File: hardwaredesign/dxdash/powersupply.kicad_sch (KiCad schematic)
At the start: 20 parts, among them J3 12V_in, U4 AMS1117-3.3, U5 TPS54302

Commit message: controller board added features
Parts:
- removed JP1: SolderJumper3V3together, Jumper:SolderJumper-2_P1.3mm_Open_TrianglePad1.0x1.5mm, symbol Jumper:SolderJumper_2_Open
- added C1: 100n, Capacitor_SMD:C_1206_3216Metric_Pad1.33x1.80mm_HandSolder, symbol Device:C_Small
- added Q7: BC556, Package_TO_SOT_THT:TO-92_Inline, symbol Transistor_BJT:BC556
- added Q8: BC546, Package_TO_SOT_THT:TO-92_Inline, symbol Transistor_BJT:BC546
- added R10, R7, R9: 4k7, Resistor_SMD:R_1206_3216Metric_Pad1.30x1.75mm_HandSolder, symbol Device:R_Small
- added R11, R12, R8: 10k, Resistor_SMD:R_1206_3216Metric_Pad1.30x1.75mm_HandSolder, symbol Device:R_Small
- added SW1: SW_Push, Button_Switch_THT:SW_PUSH_6mm_H5mm, symbol Switch:SW_Push
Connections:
- net 24V_P: now also Q7.3 (E), R9.2; no longer C67.2, U5.3 (VIN)
- net GND: now also C1.1, Q8.3 (E), R12.2, SW1.1
- new net: Q7.2 (B), R10.1, R7.2, R9.1
- new net: Q8.1 (C), R7.1
- new net: Q8.2 (B), R8.1
- new net: R10.2, R11.2, SW1.2
- new net 24V_SWITCHED: C67.2, Q7.1 (C), U5.3 (VIN)
- new net KEEP_ON: R8.2
- new net uC_pwr_button: C1.2, R11.1, R12.1
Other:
- note added: "power on/off circuit. For power-on, the power button activates the supply. The controller then can keep the power active by setting KEEP_ON. For power-off, the controller reads the power-button via a digital input, and turns-off the KEEP_ON after the button is released."
- moved on the sheet: C57, C64, C65, C66, C67, C68, C69, C70, C71, D9, J3, L13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

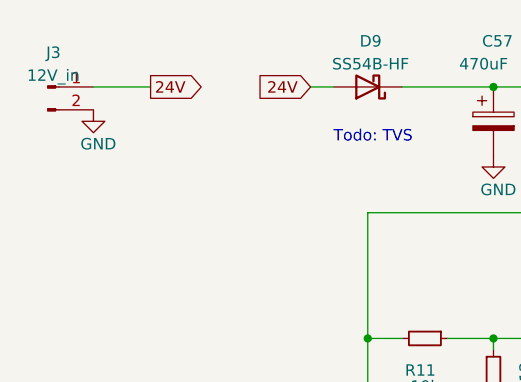
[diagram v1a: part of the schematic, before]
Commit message: added switch inputs. Layout preparation.
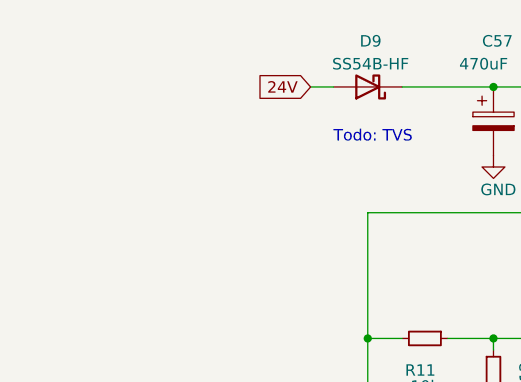
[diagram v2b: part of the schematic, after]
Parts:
- removed J3: 12V_in, Connector_PinHeader_2.54mm:PinHeader_1x02_P2.54mm_Vertical, symbol Connector:Conn_01x02_Pin
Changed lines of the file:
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@@
 	(wire
 		(pts
-			(xy 27.94 25.4) (xy 34.29 25.4)
-		)
-		(stroke
-			(width 0)
-			(type default)
-		)
-	)
-	(wire
-		(pts
 			(xy 142.24 39.37) (xy 142.24 44.45)
 		)
@@
 		)
 	)
-	(global_label "24V"
-		(shape output)
-		(at 34.29 25.4 0)
-		(fields_autoplaced yes)
-		(effects
-			(font
-				(size 1.27 1.27)
-			)
-			(justify left)
-		)
-		(property "Intersheetrefs" "${INTERSHEET_REFS}"
-			(at 40.7828 25.4 0)
-			(effects
-				(font
-					(size 1.27 1.27)
-				)
-				(justify left)
-				(hide yes)
-			)
-		)
-	)
 	(global_label "24V_SWITCHED"
 		(shape input)
@@
 	)
 	(symbol
-		(lib_id "power:GND")
-		(at 27.94 27.94 0)
-		(unit 1)
-		(exclude_from_sim no)
-		(in_bom yes)
-		(on_board yes)
-		(dnp no)
-		(property "Reference" "#PWR038"
-			(at 27.94 34.29 0)
-			(effects
-				(font
-					(size 1.27 1.27)
-				)
-				(hide yes)
-			)
-		)
-		(property "Value" "GND"
-			(at 30.48 31.75 0)
-			(effects
-				(font
-					(size 1.27 1.27)
-				)
-				(justify right)
-			)
-		)
-		(property "Footprint" ""
-			(at 27.94 27.94 0)
-			(effects
-				(font
-					(size 1.27 1.27)
-				)
-				(hide yes)
-			)
-		)
-		(property "Datasheet" ""
-			(at 27.94 27.94 0)
-			(effects
-				(font
-					(size 1.27 1.27)
-				)
-				(hide yes)
-			)
-		)
-		(property "Description" ""
-			(at 27.94 27.94 0)
-			(effects
-				(font
-					(size 1.27 1.27)
-				)
-				(hide yes)
-			)
-		)
-		(pin "1"
-		)
-		(instances
-			(project "qca7000"
-				(path "/e63e39d7-6ac0-4ffd-8aa3-1841a4541b55"
-					(reference "#PWR038")
-					(unit 1)
-				)
-				(path "/e63e39d7-6ac0-4ffd-8aa3-1841a4541b55/81db238c-e53f-4d52-98ea-36a1df697651"
-					(reference "#PWR059")
-					(unit 1)
-				)
-			)
-		)
-	)
-	(symbol
 		(lib_id "Regulator_Switching:TPS54302")
 		(at 162.56 46.99 0)
@@
 					(unit 1)
 				)
-			)
-		)
-	)
-	(symbol
-		(lib_id "Connector:Conn_01x02_Pin")
-		(at 22.86 25.4 0)
-		(unit 1)
-		(exclude_from_sim no)
-		(in_bom yes)
-		(on_board yes)
-		(dnp no)
-		(fields_autoplaced yes)
-		(property "Reference" "J3"
-			(at 23.495 21.59 0)
-			(effects
-				(font
-					(size 1.27 1.27)
-				)
-			)
-		)
-		(property "Value" "12V_in"
-			(at 23.495 24.13 0)
-			(effects
-				(font
-					(size 1.27 1.27)
-				)
-			)
-		)
-		(property "Footprint" "Connector_PinHeader_2.54mm:PinHeader_1x02_P2.54mm_Vertical"
-			(at 22.86 25.4 0)
-			(effects
-				(font
-					(size 1.27 1.27)
-				)
-				(hide yes)
-			)
-		)
-		(property "Datasheet" "~"
-			(at 22.86 25.4 0)
-			(effects
-				(font
-					(size 1.27 1.27)
-				)
-				(hide yes)
-			)
-		)
-		(property "Description" ""
-			(at 22.86 25.4 0)
-			(effects
-				(font
-					(size 1.27 1.27)
-				)
-				(hide yes)
-			)
-		)
-		(pin "1"
-		)
-		(pin "2"
-		)
-		(instances
-			(project "qca7000"
-				(path "/e63e39d7-6ac0-4ffd-8aa3-1841a4541b55"
-					(reference "J3")
-					(unit 1)
-				)
-				(path "/e63e39d7-6ac0-4ffd-8aa3-1841a4541b55/81db238c-e53f-4d52-98ea-36a1df697651"
-					(reference "J6")
-					(unit 1)
-				)

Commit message: layout work in progress
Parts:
- removed TP3V3uC1: TP3V3uC, TestPoint:TestPoint_THTPad_D1.0mm_Drill0.5mm, symbol Connector:TestPoint
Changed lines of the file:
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@@
-	)
-	(junction
-		(at 91.44 177.8)
-		(diameter 0)
-		(color 0 0 0 0)
 	)
 	(junction
@@
 	(wire
 		(pts
-			(xy 91.44 177.8) (xy 110.49 177.8)
-		)
-		(stroke
-			(width 0)
-			(type default)
-		)
-	)
-	(wire
-		(pts
 			(xy 58.42 39.37) (xy 106.68 39.37)
 		)
@@
 	(wire
 		(pts
-			(xy 85.09 177.8) (xy 91.44 177.8)
+			(xy 85.09 177.8) (xy 110.49 177.8)
 		)
 		(stroke
@@
 					(unit 1)
 				)
-			)
-		)
-	)
-	(symbol
-		(lib_id "Connector:TestPoint")
-		(at 91.44 177.8 0)
-		(unit 1)
-		(exclude_from_sim no)
-		(in_bom yes)
-		(on_board yes)
-		(dnp no)
-		(property "Reference" "TP3V3uC1"
-			(at 90.17 170.18 0)
-			(effects
-				(font
-					(size 1.27 1.27)
-				)
-				(justify left)
-			)
-		)
-		(property "Value" "TP3V3uC"
-			(at 90.17 172.72 0)
-			(effects
-				(font
-					(size 1.27 1.27)
-				)
-				(justify left)
-			)
-		)
-		(property "Footprint" "TestPoint:TestPoint_THTPad_D1.0mm_Drill0.5mm"
-			(at 96.52 177.8 0)
-			(effects
-				(font
-					(size 1.27 1.27)
-				)
-				(hide yes)
-			)
-		)
-		(property "Datasheet" "~"
-			(at 96.52 177.8 0)
-			(effects
-				(font
-					(size 1.27 1.27)
-				)
-				(hide yes)
-			)
-		)
-		(property "Description" ""
-			(at 91.44 177.8 0)
-			(effects
-				(font
-					(size 1.27 1.27)
-				)
-				(hide yes)
-			)
-		)
-		(pin "1"
-		)
-		(instances
-			(project "qca7000"
-				(path "/e63e39d7-6ac0-4ffd-8aa3-1841a4541b55"
-					(reference "TP3V3uC1")
-					(unit 1)
-				)
-				(path "/e63e39d7-6ac0-4ffd-8aa3-1841a4541b55/81db238c-e53f-4d52-98ea-36a1df697651"
-					(reference "TP3V3uC1")
-					(unit 1)
-				)

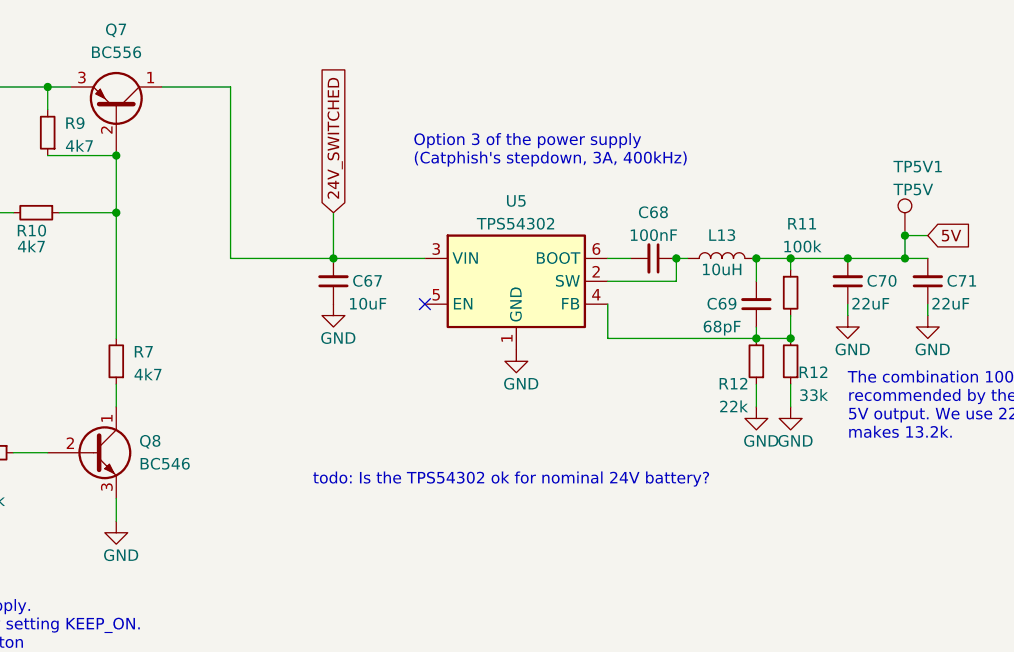
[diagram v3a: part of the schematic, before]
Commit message: board: layout finished
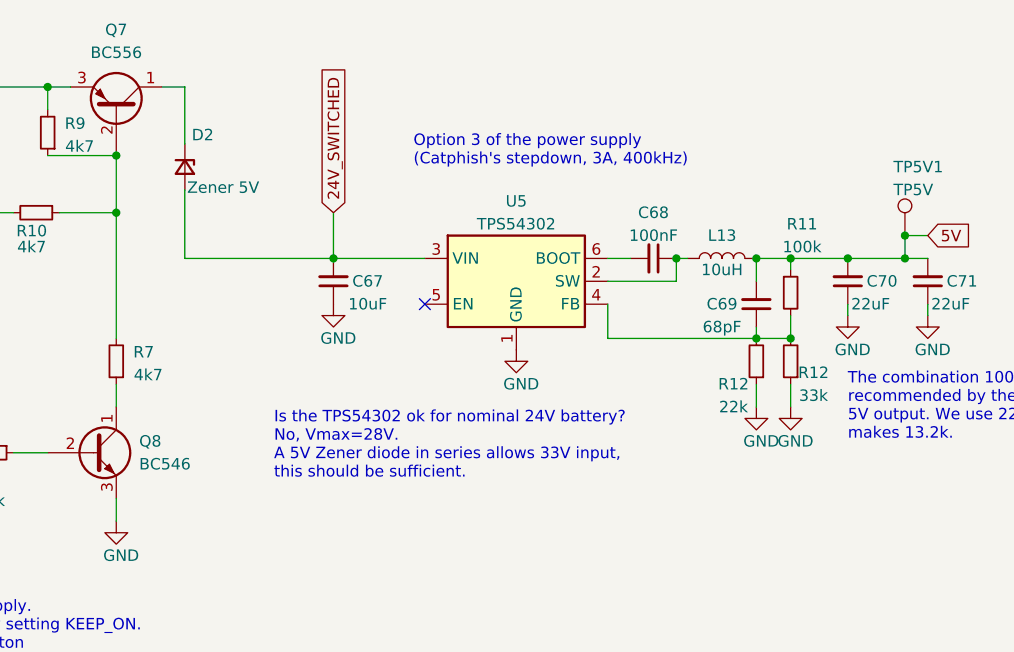
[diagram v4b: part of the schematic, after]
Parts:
- added D2: Zener 5V, Diode_THT:D_DO-201_P15.24mm_Horizontal, symbol Device:D_Zener_Small
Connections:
- net 24V_SWITCHED: now also D2.2 (A); no longer Q7.1 (C)
- new net: D2.1 (K), Q7.1 (C)
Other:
- note added: "Is the TPS54302 ok for nominal 24V battery? No, Vmax=28V. A 5V Zener diode in series allows 33V input, this should be sufficient."
- note removed: "todo: Is the TPS54302 ok for nominal 24V battery?"
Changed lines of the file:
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@@
+	(wire
+		(pts
+			(xy 125.73 25.4) (xy 125.73 31.75)
+		)
+		(stroke
+			(width 0)
+			(type default)
+		)
+	)
 	(wire
 		(pts
@@
 	(wire
 		(pts
-			(xy 130.81 25.4) (xy 130.81 44.45)
-		)
-		(stroke
-			(width 0)
-			(type default)
-		)
-	)
-	(wire
-		(pts
 			(xy 82.55 53.34) (xy 86.36 53.34)
 		)
@@
 	(wire
 		(pts
-			(xy 142.24 44.45) (xy 130.81 44.45)
+			(xy 142.24 44.45) (xy 125.73 44.45)
 		)
 		(stroke
@@
 	(wire
 		(pts
+			(xy 125.73 36.83) (xy 125.73 44.45)
+		)
+		(stroke
+			(width 0)
+			(type default)
+		)
+	)
+	(wire
+		(pts
 			(xy 118.11 58.42) (xy 118.11 60.96)
 		)
@@
 	(wire
 		(pts
-			(xy 123.19 25.4) (xy 130.81 25.4)
+			(xy 123.19 25.4) (xy 125.73 25.4)
 		)
 		(stroke
@@
 		)
 	)
-	(text "todo: Is the TPS54302 ok for nominal 24V battery?"
-		(exclude_from_sim no)
-		(at 139.954 69.85 0)
+	(text "Is the TPS54302 ok for nominal 24V battery?\nNo, Vmax=28V.\nA 5V Zener diode in series allows 33V input,\nthis should be sufficient."
+		(exclude_from_sim no)
+		(at 135.636 69.088 0)
 		(effects
 			(font
@@
 					(unit 1)
 				)
+			)
+		)
+	)
+	(symbol
+		(lib_id "Device:D_Zener_Small")
+		(at 125.73 34.29 270)
+		(unit 1)
+		(exclude_from_sim no)
+		(in_bom yes)
+		(on_board yes)
+		(dnp no)
+		(property "Reference" "D2"
+			(at 126.492 30.734 90)
+			(effects
+				(font
+					(size 1.27 1.27)
+				)
+				(justify left)
+			)
+		)
+		(property "Value" "Zener 5V"
+			(at 125.984 36.576 90)
+			(effects
+				(font
+					(size 1.27 1.27)
+				)
+				(justify left)
+			)
+		)
+		(property "Footprint" "Diode_THT:D_DO-201_P15.24mm_Horizontal"
+			(at 125.73 34.29 90)
+			(effects
+				(font
+					(size 1.27 1.27)
+				)
+				(hide yes)
+			)
+		)
+		(property "Datasheet" "~"
+			(at 125.73 34.29 90)
+			(effects
+				(font
+					(size 1.27 1.27)
+				)
+				(hide yes)
+			)
+		)
+		(property "Description" "Zener diode, small symbol"
+			(at 125.73 34.29 0)
+			(effects
+				(font
+					(size 1.27 1.27)
+				)
+				(hide yes)
+			)
+		)
+		(pin "2"
+		)
+		(pin "1"
+		)
+		(instances
+			(project ""
+				(path "/e63e39d7-6ac0-4ffd-8aa3-1841a4541b55/81db238c-e53f-4d52-98ea-36a1df697651"
+					(reference "D2")
+					(unit 1)
+				)

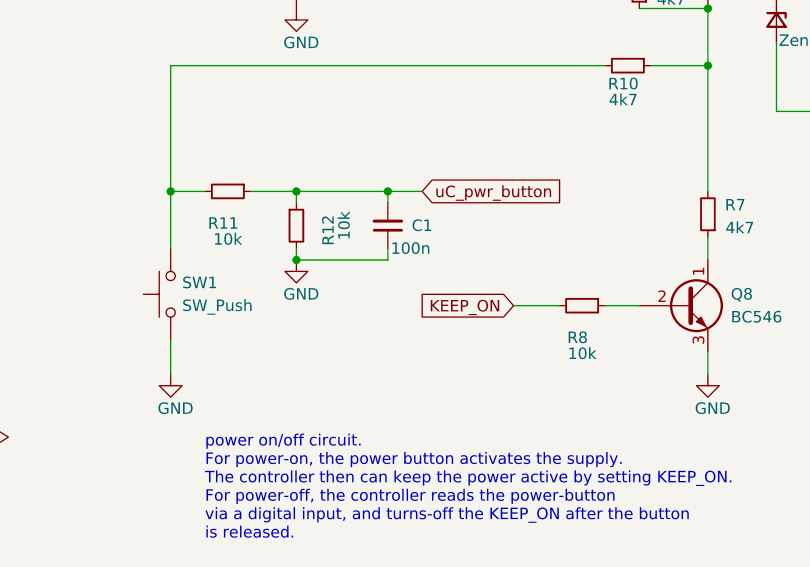
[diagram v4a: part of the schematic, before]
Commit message: dxdash: corrected some resistor values. Added todos.
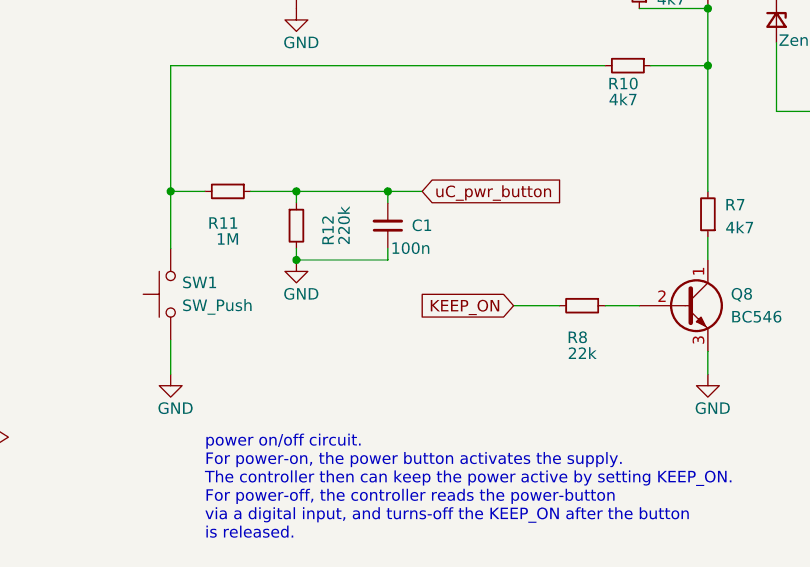
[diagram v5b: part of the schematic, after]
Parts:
- R11: value 10k -> 1M; LCSC C22978 -> (none)
- R12: value 10k -> 220k; LCSC C22978 -> (none)
- R8: value 10k -> 22k; LCSC C22978 -> (none)
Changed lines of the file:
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@@
 			)
 		)
-		(property "Value" "10k"
+		(property "Value" "220k"
 			(at 77.724 57.15 90)
 			(effects
@@
 			)
 		)
-		(property "Datasheet" "https://datasheet.lcsc.com/lcsc/1811101920_UNI-ROYAL-Uniroyal-Elec-0603WAF3301T5E_C22978.pdf"
+		(property "Datasheet" ""
 			(at 72.39 57.15 0)
 			(effects
@@
 			)
 		)
-		(property "LCSC" "C22978"
+		(property "LCSC" ""
 			(at 72.39 57.15 90)
 			(effects
@@
 			)
 		)
-		(property "Value" "10k"
+		(property "Value" "1M"
 			(at 64.77 58.674 90)
 			(effects
@@
 			)
 		)
-		(property "Datasheet" "https://datasheet.lcsc.com/lcsc/1811101920_UNI-ROYAL-Uniroyal-Elec-0603WAF3301T5E_C22978.pdf"
+		(property "Datasheet" ""
 			(at 64.77 53.34 0)
 			(effects
@@
 			)
 		)
-		(property "LCSC" "C22978"
+		(property "LCSC" ""
 			(at 64.77 53.34 90)
 			(effects
@@
 			)
 		)
-		(property "Value" "10k"
+		(property "Value" "22k"
 			(at 104.14 71.374 90)
 			(effects
@@
 			)
 		)
-		(property "Datasheet" "https://datasheet.lcsc.com/lcsc/1811101920_UNI-ROYAL-Uniroyal-Elec-0603WAF3301T5E_C22978.pdf"
+		(property "Datasheet" ""
 			(at 104.14 66.04 0)
 			(effects
@@
 			)
 		)
-		(property "LCSC" "C22978"
+		(property "LCSC" ""
 			(at 104.14 66.04 90)
 			(effects
